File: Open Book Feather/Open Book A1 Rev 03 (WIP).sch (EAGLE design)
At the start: 126 parts, among them J1 SJ-43514-SMT, J2 10118193-0001LF, Q1 DMG341, Q2 IRLML0100, SW1 SPDT_SWITCH, U1 AP2112-3.3, U2 MCP73831T-2ACI/OT, U3 ATSAMD51J64-TQFP(10X10), U4 GD25Q16C (or GD25Q32C), U5 MCP23008/SO, U6 GD25Q16C (or GD25Q32C), U8 MAX4466EXK+T, X1 JSTPH, X2 2x5 0.05" SWD

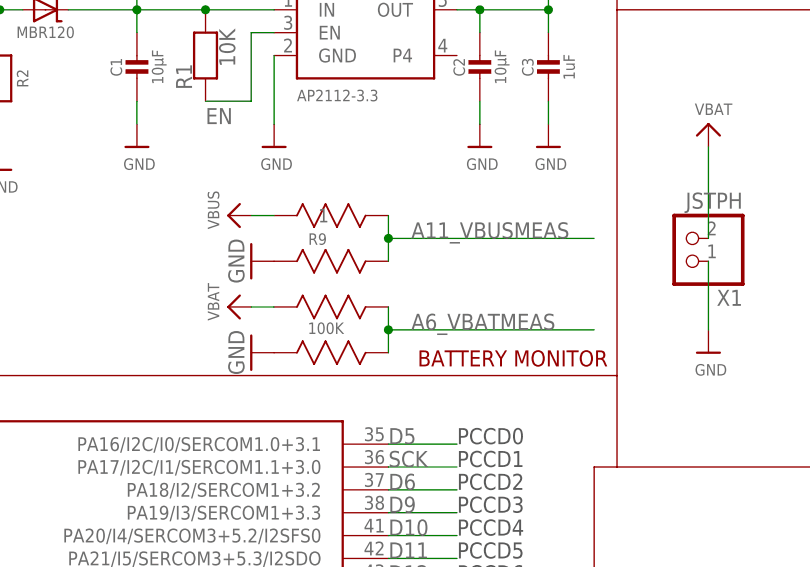
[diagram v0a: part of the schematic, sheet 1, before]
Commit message: maybe power and gnd pads shouldn't be so close together
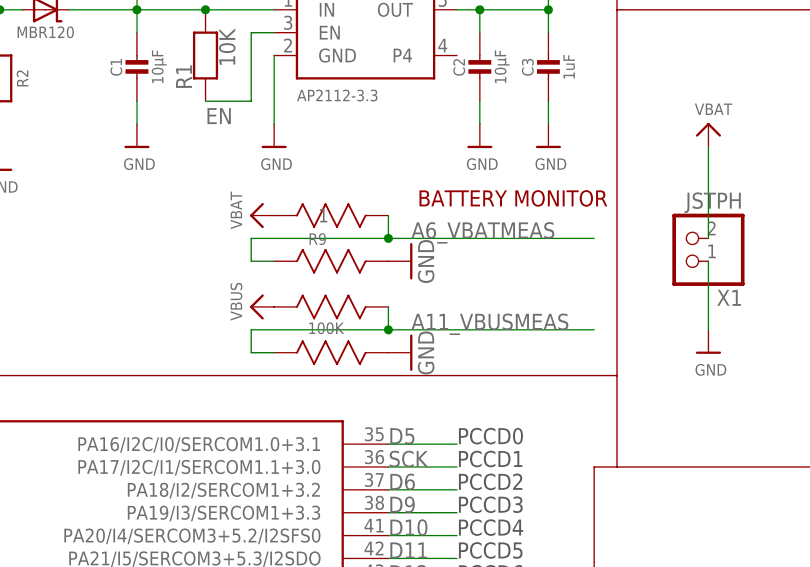
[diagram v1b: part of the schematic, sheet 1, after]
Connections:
- net A11_VBUSMEAS: now also R9.4, R9.6; no longer R9.7, R9.8
- net A6_VBATMEAS: now also R9.2, R9.8; no longer R9.5, R9.6
- net GND: now also R9.5, R9.7; no longer R9.2, R9.4
- net VBAT: now also R9.1; no longer R9.3
- net VBUS: now also R9.3; no longer R9.1
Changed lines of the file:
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@@
 <part name="R14" library="microbuilder" deviceset="RESISTOR" device="_0805MP" value="10K"/>
 <part name="R9" library="resistor array" deviceset="EXB-V8V103JV" device="" value="100K"/>
-<part name="GND9" library="supply1" library_urn="urn:adsk.eagle:library:371" deviceset="GND" device=""/>
-<part name="GND12" library="supply1" library_urn="urn:adsk.eagle:library:371" deviceset="GND" device=""/>
-<part name="U$46" library="microbuilder" deviceset="VBUS" device=""/>
-<part name="U$23" library="microbuilder" deviceset="VBAT" device=""/>
 <part name="FUL" library="adafruit" deviceset="LED" device="CHIP-LED0805" value="GREEN"/>
 <part name="R5" library="microbuilder" deviceset="RESISTOR" device="0805_NOOUTLINE" value="1K"/>
 <part name="U$34" library="microbuilder" deviceset="GND" device=""/>
 <part name="U$49" library="microbuilder" deviceset="VBUS" device=""/>
+<part name="GND9" library="supply1" library_urn="urn:adsk.eagle:library:371" deviceset="GND" device=""/>
+<part name="GND12" library="supply1" library_urn="urn:adsk.eagle:library:371" deviceset="GND" device=""/>
+<part name="U$50" library="microbuilder" deviceset="VBUS" device=""/>
+<part name="U$51" library="microbuilder" deviceset="VBAT" device=""/>
 </parts>
 <sheets>
@@
 * Power MOSFET for bright white LED's?
 ✓ VUSB to a pin via voltage divider.</text>
-<text x="461.264" y="106.934" size="1.778" layer="94" rot="R180">BATTERY MONITOR</text>
+<text x="461.264" y="124.714" size="1.778" layer="94" rot="R180">BATTERY MONITOR</text>
 <text x="434.34" y="12.7" size="1.778" layer="88">Available (interrupt)</text>
 <text x="434.34" y="38.1" size="1.778" layer="88">Available (interrupt)</text>
@@
 <attribute name="NAME" x="427.9646" y="118.6688" size="1.27" layer="95" ratio="10" rot="SR0"/>
 </instance>
-<instance part="GND9" gate="1" x="421.64" y="116.84" smashed="yes" rot="R270">
-<attribute name="VALUE" x="419.1" y="119.38" size="1.778" layer="96" rot="R270"/>
-</instance>
-<instance part="GND12" gate="1" x="421.64" y="106.68" smashed="yes" rot="R270">
-<attribute name="VALUE" x="419.1" y="109.22" size="1.778" layer="96" rot="R270"/>
-</instance>
-<instance part="U$46" gate="G$1" x="419.1" y="121.92" smashed="yes" rot="R90">
-<attribute name="VALUE" x="418.084" y="120.396" size="1.27" layer="96" rot="R90"/>
-</instance>
-<instance part="U$23" gate="G$1" x="419.1" y="111.76" smashed="yes" rot="R90">
-<attribute name="VALUE" x="418.084" y="110.236" size="1.27" layer="96" rot="R90"/>
-</instance>
 <instance part="FUL" gate="G$1" x="495.3" y="104.14" smashed="yes" rot="R270">
 <attribute name="NAME" x="495.808" y="105.664" size="1.778" layer="95"/>
@@
 <instance part="U$49" gate="G$1" x="487.68" y="121.92" smashed="yes">
 <attribute name="VALUE" x="486.156" y="122.936" size="1.27" layer="96"/>
+</instance>
+<instance part="GND9" gate="1" x="439.42" y="116.84" smashed="yes" rot="R90">
+<attribute name="VALUE" x="441.96" y="114.3" size="1.778" layer="96" rot="R90"/>
+</instance>
+<instance part="GND12" gate="1" x="439.42" y="106.68" smashed="yes" rot="R90">
+<attribute name="VALUE" x="441.96" y="104.14" size="1.778" layer="96" rot="R90"/>
+</instance>
+<instance part="U$50" gate="G$1" x="421.64" y="111.76" smashed="yes" rot="R90">
+<attribute name="VALUE" x="420.624" y="110.236" size="1.27" layer="96" rot="R90"/>
+</instance>
+<instance part="U$51" gate="G$1" x="421.64" y="121.92" smashed="yes" rot="R90">
+<attribute name="VALUE" x="420.624" y="120.396" size="1.27" layer="96" rot="R90"/>
 </instance>
 </instances>
@@
 </segment>
 <segment>
-<pinref part="R9" gate="A" pin="2"/>
-<pinref part="GND9" gate="1" pin="GND"/>
-</segment>
-<segment>
-<pinref part="R9" gate="A" pin="4"/>
-<pinref part="GND12" gate="1" pin="GND"/>
-</segment>
-<segment>
 <pinref part="FUL" gate="G$1" pin="C"/>
 <wire x1="490.22" y1="104.14" x2="487.68" y2="104.14" width="0.1524" layer="91"/>
 <wire x1="487.68" y1="104.14" x2="487.68" y2="101.6" width="0.1524" layer="91"/>
 <pinref part="U$34" gate="G$1" pin="GND"/>
+</segment>
+<segment>
+<pinref part="R9" gate="A" pin="7"/>
+<pinref part="GND9" gate="1" pin="GND"/>
+</segment>
+<segment>
+<pinref part="R9" gate="A" pin="5"/>
+<pinref part="GND12" gate="1" pin="GND"/>
 </segment>
 </net>
@@
 </segment>
 <segment>
-<pinref part="U$23" gate="G$1" pin="VBAT"/>
-<wire x1="421.64" y1="111.76" x2="424.18" y2="111.76" width="0.1524" layer="91"/>
-<pinref part="R9" gate="A" pin="3"/>
+<pinref part="R9" gate="A" pin="1"/>
+<pinref part="U$51" gate="G$1" pin="VBAT"/>
 </segment>
 </net>
@@
 </segment>
 <segment>
-<wire x1="459.74" y1="109.22" x2="436.88" y2="109.22" width="0.1524" layer="91"/>
-<label x="439.42" y="109.22" size="1.778" layer="95"/>
-<pinref part="R9" gate="A" pin="6"/>
-<wire x1="436.88" y1="111.76" x2="436.88" y2="109.22" width="0.1524" layer="91"/>
-<pinref part="R9" gate="A" pin="5"/>
-<wire x1="436.88" y1="109.22" x2="436.88" y2="106.68" width="0.1524" layer="91"/>
-<junction x="436.88" y="109.22"/>
+<wire x1="436.88" y1="119.38" x2="459.74" y2="119.38" width="0.1524" layer="91"/>
+<label x="439.42" y="119.38" size="1.778" layer="95"/>
+<pinref part="R9" gate="A" pin="8"/>
+<wire x1="436.88" y1="121.92" x2="436.88" y2="119.38" width="0.1524" layer="91"/>
+<pinref part="R9" gate="A" pin="2"/>
+<wire x1="424.18" y1="116.84" x2="421.64" y2="116.84" width="0.1524" layer="91"/>
+<wire x1="421.64" y1="116.84" x2="421.64" y2="119.38" width="0.1524" layer="91"/>
+<wire x1="421.64" y1="119.38" x2="436.88" y2="119.38" width="0.1524" layer="91"/>
+<junction x="436.88" y="119.38"/>
 </segment>
 </net>
@@
 </segment>
 <segment>
-<pinref part="U$46" gate="G$1" pin="VBUS"/>
-<wire x1="421.64" y1="121.92" x2="424.18" y2="121.92" width="0.1524" layer="91"/>
-<pinref part="R9" gate="A" pin="1"/>
+<pinref part="R9" gate="A" pin="3"/>
+<pinref part="U$50" gate="G$1" pin="VBUS"/>
 </segment>
 </net>
@@
 </segment>
 <segment>
-<wire x1="436.88" y1="119.38" x2="459.74" y2="119.38" width="0.1524" layer="91"/>
-<label x="439.42" y="119.38" size="1.778" layer="95"/>
-<pinref part="R9" gate="A" pin="8"/>
-<wire x1="436.88" y1="121.92" x2="436.88" y2="119.38" width="0.1524" layer="91"/>
-<pinref part="R9" gate="A" pin="7"/>
-<wire x1="436.88" y1="119.38" x2="436.88" y2="116.84" width="0.1524" layer="91"/>
-<junction x="436.88" y="119.38"/>
-</segment>
-</net>
+<wire x1="459.74" y1="109.22" x2="436.88" y2="109.22" width="0.1524" layer="91"/>
+<label x="439.42" y="109.22" size="1.778" layer="95"/>
+<pinref part="R9" gate="A" pin="6"/>
+<wire x1="436.88" y1="111.76" x2="436.88" y2="109.22" width="0.1524" layer="91"/>
+<pinref part="R9" gate="A" pin="4"/>
+<wire x1="424.18" y1="106.68" x2="421.64" y2="106.68" width="0.1524" layer="91"/>
+<wire x1="421.64" y1="106.68" x2="421.64" y2="109.22" width="0.1524" layer="91"/>
+<wire x1="421.64" y1="109.22" x2="436.88" y2="109.22" width="0.1524" layer="91"/>
+<junction x="436.88" y="109.22"/>
+</segment>
+</net>
